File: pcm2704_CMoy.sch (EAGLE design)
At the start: 85 parts, among them IC3 7815DT, IC4 tsr 1-2433, IC5 7915TV, Q1 12MHz, U1 PCM2704, U2 OPA2134P, U3 TC962EPA, X2 PN61729-S, X5 22-23-2031, X6 22-23-2031

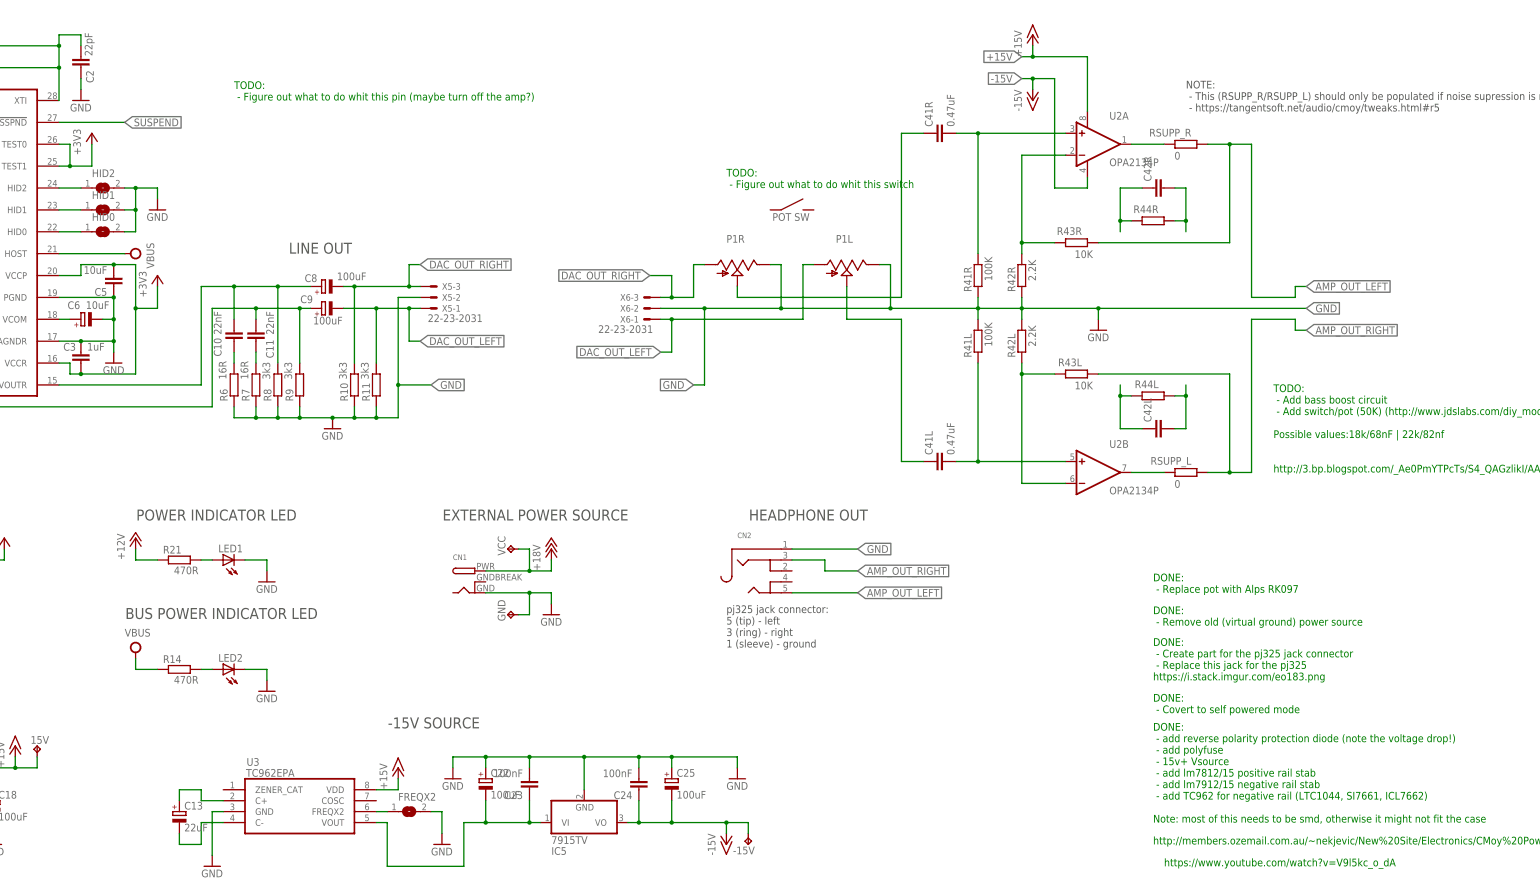
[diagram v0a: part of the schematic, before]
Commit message: - Added resistor between the wiper and ground of the volume pot
 - Fixed the pot direction
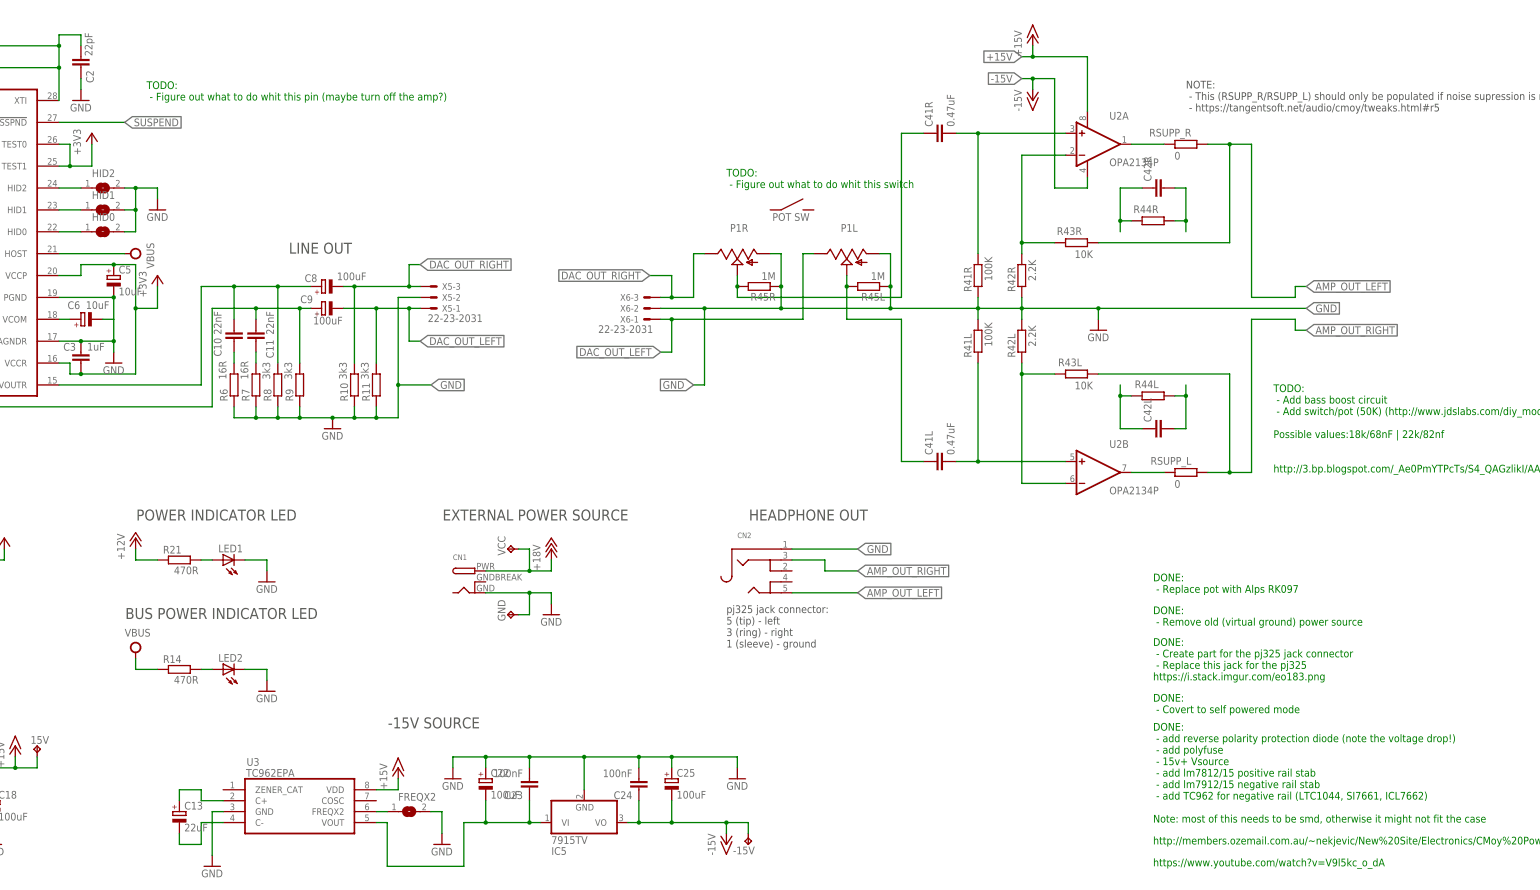
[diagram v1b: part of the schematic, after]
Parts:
- added R45L, R45R: 1M, rcl:R-EU_0204/7
- C5: device rcl:C-EUC0805 -> qfm-trx1-24g:CPOL-EUE2.5-7
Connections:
- net +3V3: now also C5.+; no longer C5.2
- net DAC_OUT_LEFT: now also P1L.3; no longer P1L.1
- net DAC_OUT_RIGHT: now also P1R.3; no longer P1R.1
- net GND: now also C5.-, P1L.1, P1R.1, R45L.1, R45R.1; no longer C5.1, P1L.3, P1R.3
- net N$19: now also R45R.2
- net N$21: now also R45L.2
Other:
- moved on the sheet: P1L, P1R
